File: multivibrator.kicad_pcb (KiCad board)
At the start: 2 copper layers, 47 x 31.8 mm, 11 parts, among them CON1 BARREL_JACK, Q1 Q_NPN_BCE, Q2 Q_NPN_BCE

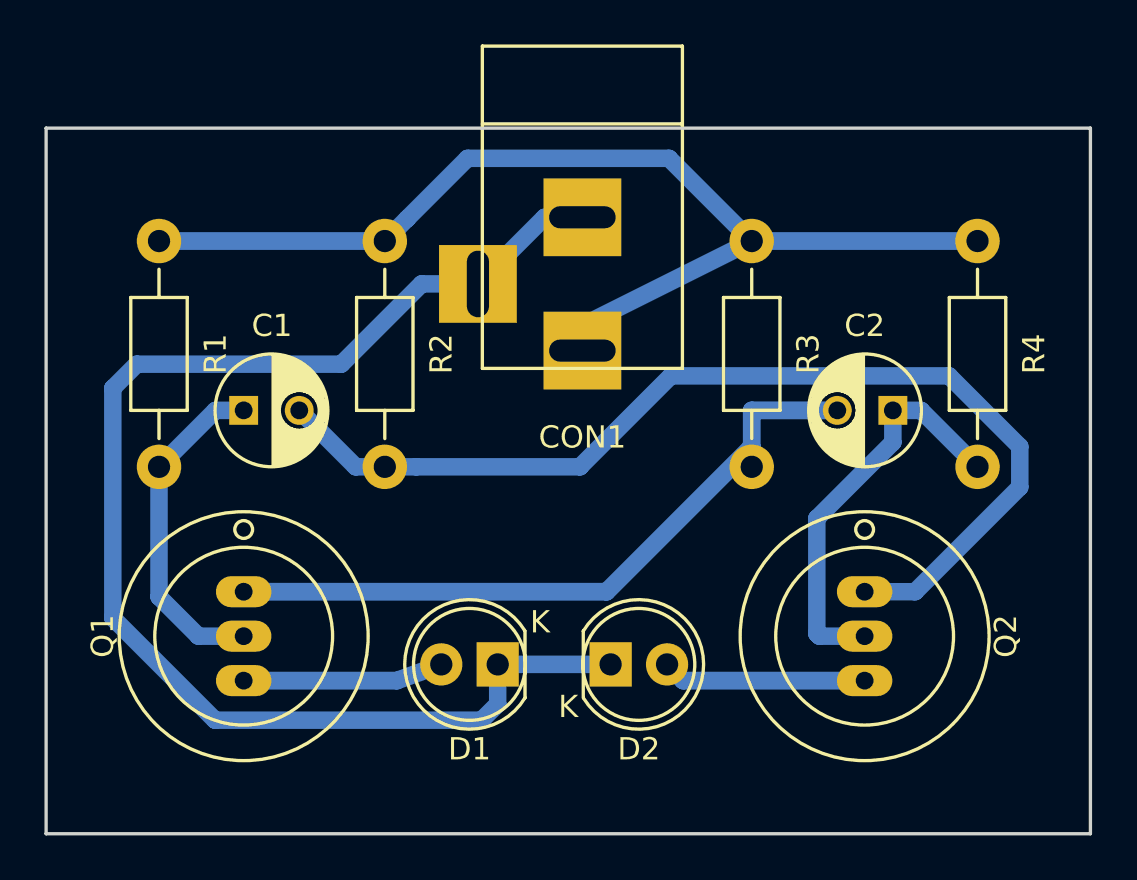
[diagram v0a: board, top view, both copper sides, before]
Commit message: ebc npn transistors laid out
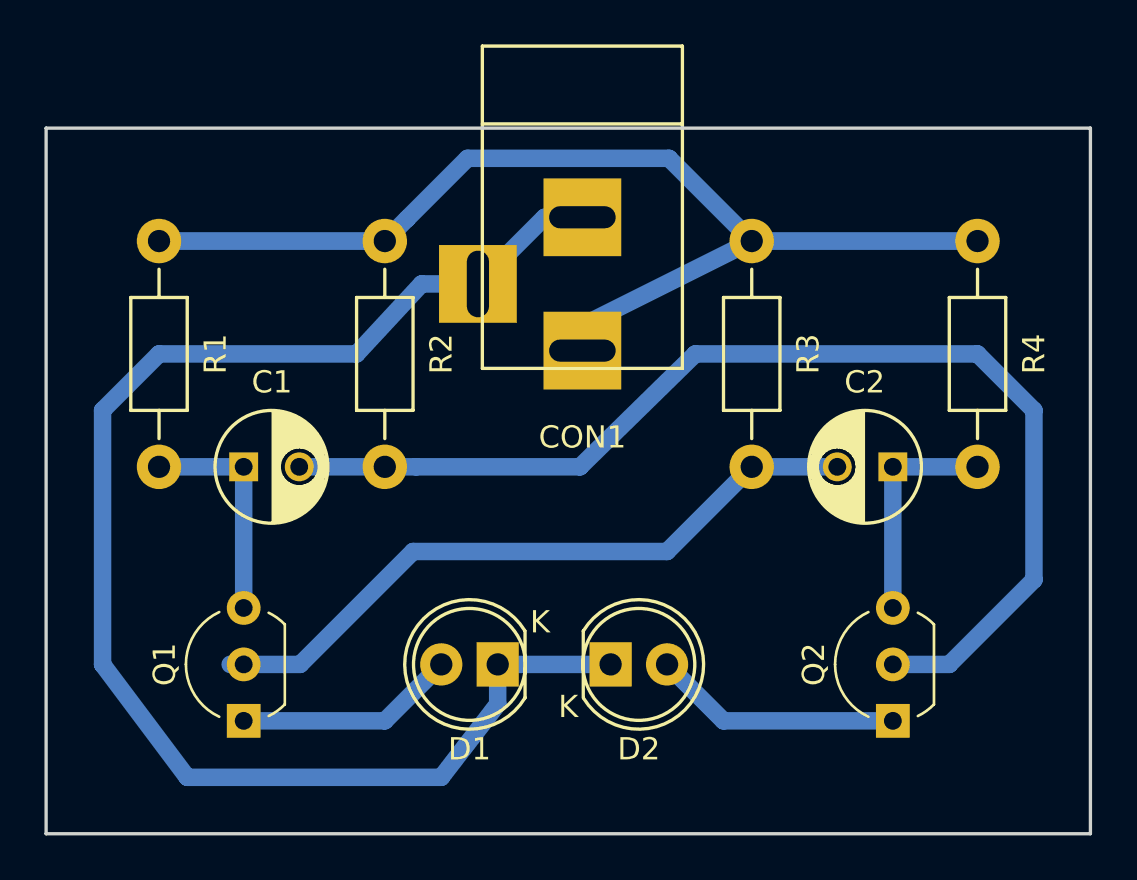
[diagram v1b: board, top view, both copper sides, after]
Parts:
- Q1, Q2: value Q_NPN_BCE -> Q_NPN_EBC; footprint Transistors_OldSowjetAera:OldSowjetaera_Transistor_Type-I_BigPads -> TO_SOT_Packages_THT:TO-92_Inline_Wide
- moved Q2 4.02 mm to (115.6, 86.4), turned to 90 degrees
- moved Q1 3.81 mm to (86.4, 86.4), turned to 90 degrees
- moved C1 2.54 mm to (86.4, 74.9)
- moved C2 2.54 mm to (115.6, 74.9)
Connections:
- Q1 pad 1: Net-(C2-Pad2) -> Net-(D1-Pad2)
- Q1 pad 2: Net-(C1-Pad1) -> Net-(C2-Pad2)
- Q1 pad 3: Net-(D1-Pad2) -> Net-(C1-Pad1)
- Q2 pad 1: Net-(C1-Pad2) -> Net-(D2-Pad2)
- Q2 pad 2: Net-(C2-Pad1) -> Net-(C1-Pad2)
- Q2 pad 3: Net-(D2-Pad2) -> Net-(C2-Pad1)
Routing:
- net Net-(C2-Pad1): track 18.5 -> 10.2 mm
- net Net-(C1-Pad1): track 15.9 -> 10.2 mm
- net Net-(C1-Pad2): track 47.2 -> 51.7 mm
- net GND: track 61.0 -> 65.5 mm
- net Net-(D2-Pad2): track 9.19 -> 11.2 mm
- net Net-(D1-Pad2): track 9.02 -> 9.94 mm

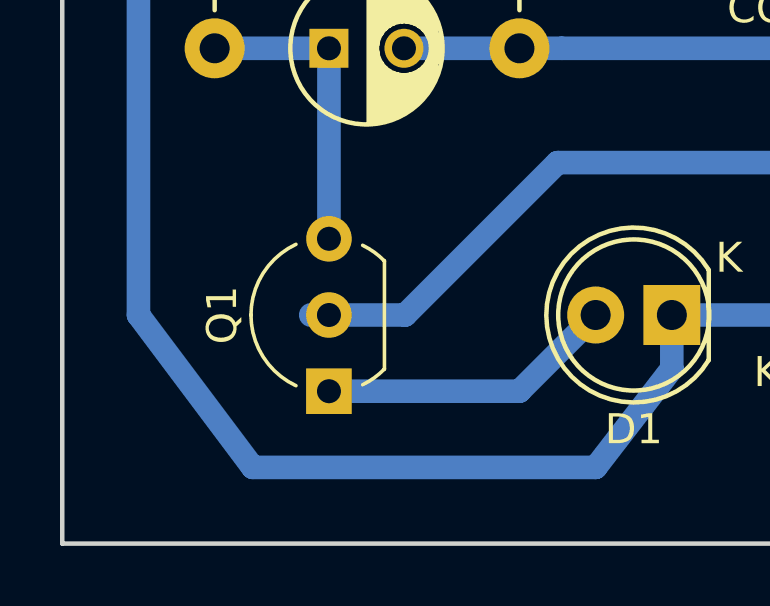
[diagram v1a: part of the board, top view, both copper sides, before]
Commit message: clean up a tiny track on pcb and regen cnc
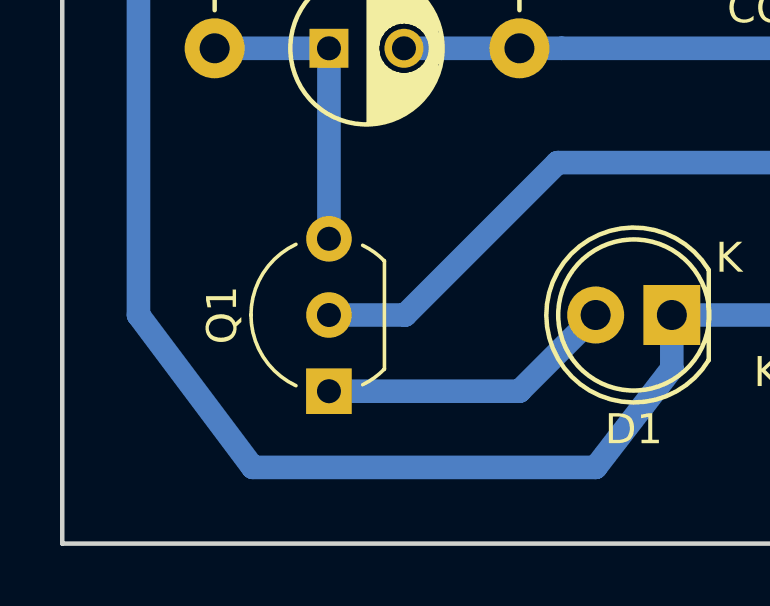
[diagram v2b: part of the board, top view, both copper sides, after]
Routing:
- net Net-(C2-Pad2): track 31.0 -> 30.4 mm
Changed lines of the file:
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@@
     (links 17)
     (no_connects 0)
-    (area 77.394999 59.614999 124.535001 91.515001)
+    (area 77.394999 55.416379 124.535001 91.515001)
     (thickness 1.6)
     (drawings 4)
-    (tracks 43)
+    (tracks 42)
     (zones 0)
     (modules 11)
@@
     (visible_elements FFFFFF7F)
     (pcbplotparams
-      (layerselection 0x00020_80000001)
+      (layerselection 0x01020_80000000)
       (usegerberextensions false)
       (excludeedgelayer true)
@@
       (drillshape 0)
       (scaleselection 1)
-      (outputdirectory svg/))
+      (outputdirectory gerbers/))
   )
   (net 0 "")
@@
   (segment (start 82.55 74.93) (end 86.36 74.93) (width 0.7874) (layer B.Cu) (net 2))
   (segment (start 86.36 74.93) (end 86.36 81.28) (width 0.7874) (layer B.Cu) (net 2) (status 10))
+  (segment (start 109.22 74.93) (end 105.41 78.74) (width 0.7874) (layer B.Cu) (net 3))
+  (segment (start 105.41 78.74) (end 93.98 78.74) (width 0.7874) (layer B.Cu) (net 3))
+  (segment (start 93.98 78.74) (end 88.9 83.82) (width 0.7874) (layer B.Cu) (net 3))
+  (segment (start 88.9 83.82) (end 86.36 83.82) (width 0.7874) (layer B.Cu) (net 3))
   (segment (start 113.07 74.93) (end 109.22 74.93) (width 0.7874) (layer B.Cu) (net 3))
-  (segment (start 109.22 74.93) (end 105.41 78.74) (width 0.7874) (layer B.Cu) (net 3))
-  (segment (start 88.9 83.82) (end 86.36 83.82) (width 0.7874) (layer B.Cu) (net 3))
-  (segment (start 93.98 78.74) (end 88.9 83.82) (width 0.7874) (layer B.Cu) (net 3))
-  (segment (start 105.41 78.74) (end 93.98 78.74) (width 0.7874) (layer B.Cu) (net 3))
-  (segment (start 85.758571 83.82) (end 86.36 83.82) (width 0.8001) (layer B.Cu) (net 3) (status 30))
   (segment (start 119.38 74.93) (end 115.57 74.93) (width 0.7874) (layer B.Cu) (net 4))
   (segment (start 115.57 74.93) (end 115.57 81.28) (width 0.7874) (layer B.Cu) (net 4) (status 10))
